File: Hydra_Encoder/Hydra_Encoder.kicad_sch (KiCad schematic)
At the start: 10 parts, among them IC101 AS5600-ASOT, J101 Conn_01x04

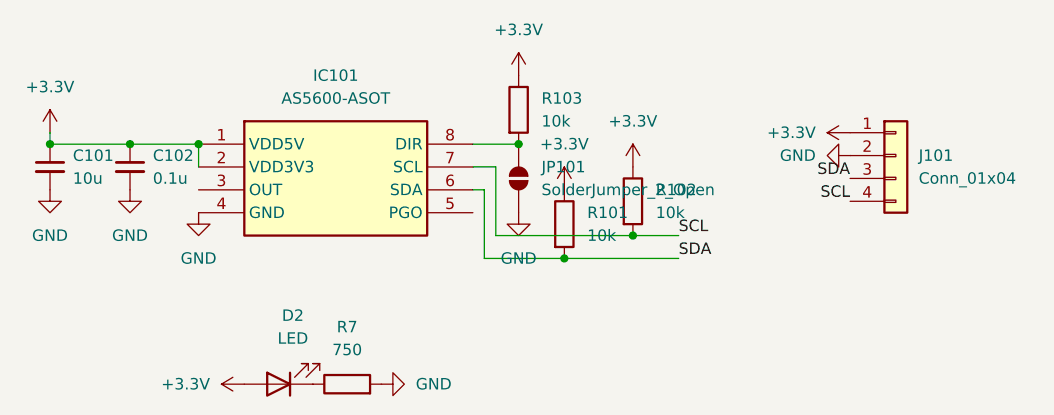
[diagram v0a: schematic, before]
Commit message: Fixed issues preparing for build
Fixed XT30 connectors on Hydra_Driver reversed, fixed I2C connector pin order, refined silkscreens
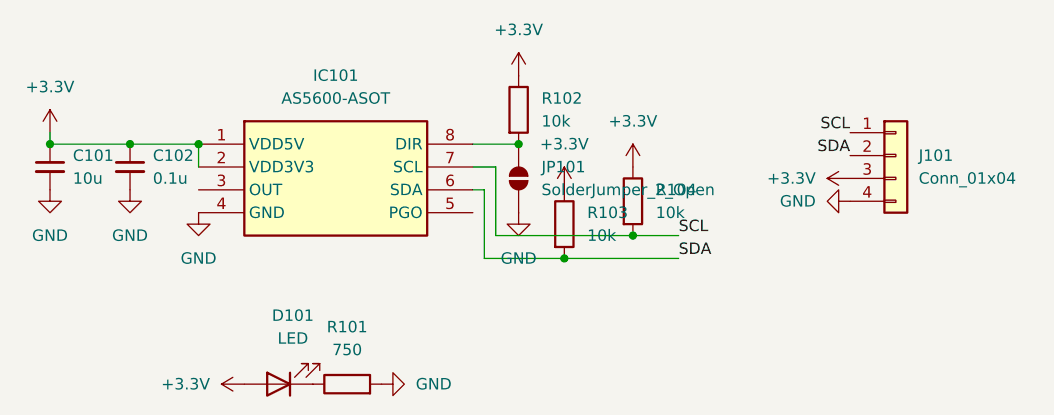
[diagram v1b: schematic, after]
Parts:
- renumbered D2 to D101, R7 to R101, R103 to R102, R101 to R103, R102 to R104
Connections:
- net +3.3V: now also J101.3 (Pin_3); no longer J101.1 (Pin_1)
- net GND: now also J101.4 (Pin_4); no longer J101.2 (Pin_2)
- net SCL: now also J101.1 (Pin_1); no longer J101.4 (Pin_4)
- net SDA: now also J101.2 (Pin_2); no longer J101.3 (Pin_3)
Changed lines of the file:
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@@
 	)
 	(label "SDA"
-		(at 115.57 39.37 180)
+		(at 115.57 36.83 180)
 		(effects
 			(font
@@
 	)
 	(label "SCL"
-		(at 115.57 41.91 180)
+		(at 115.57 34.29 180)
 		(effects
 			(font
@@
 		(dnp no)
 		(fields_autoplaced yes)
-		(property "Reference" "R101"
+		(property "Reference" "R103"
 			(at 86.36 43.1799 0)
 			(effects
@@
 			(project ""
 				(path "/e16511bf-512b-475d-aead-9861d1dac631"
-					(reference "R101")
+					(reference "R103")
 					(unit 1)
 				)
@@
 		(dnp no)
 		(fields_autoplaced yes)
-		(property "Reference" "#PWR0104"
+		(property "Reference" "#PWR0109"
 			(at 83.82 44.45 0)
 			(effects
@@
 			(project ""
 				(path "/e16511bf-512b-475d-aead-9861d1dac631"
-					(reference "#PWR0104")
+					(reference "#PWR0109")
 					(unit 1)
 				)
@@
 		(dnp no)
 		(fields_autoplaced yes)
-		(property "Reference" "#PWR0111"
+		(property "Reference" "#PWR0105"
 			(at 52.07 62.23 0)
 			(effects
@@
 			(project "Hydra_Encoder"
 				(path "/e16511bf-512b-475d-aead-9861d1dac631"
-					(reference "#PWR0111")
+					(reference "#PWR0105")
 					(unit 1)
 				)
@@
 		(dnp no)
 		(fields_autoplaced yes)
-		(property "Reference" "#PWR0108"
+		(property "Reference" "#PWR0103"
 			(at 35.56 46.99 0)
 			(effects
@@
 			(project "Hydra_Encoder"
 				(path "/e16511bf-512b-475d-aead-9861d1dac631"
-					(reference "#PWR0108")
+					(reference "#PWR0103")
 					(unit 1)
 				)
@@
 		(dnp no)
 		(fields_autoplaced yes)
-		(property "Reference" "R7"
+		(property "Reference" "R101"
 			(at 59.69 55.88 90)
 			(effects
@@
 			(project "Hydra_Encoder"
 				(path "/e16511bf-512b-475d-aead-9861d1dac631"
-					(reference "R7")
+					(reference "R101")
 					(unit 1)
 				)
@@
 		(dnp no)
 		(fields_autoplaced yes)
-		(property "Reference" "#PWR0106"
+		(property "Reference" "#PWR0108"
 			(at 78.74 49.53 0)
 			(effects
@@
 			(project "Hydra_Encoder"
 				(path "/e16511bf-512b-475d-aead-9861d1dac631"
-					(reference "#PWR0106")
+					(reference "#PWR0108")
 					(unit 1)
 				)
@@
 		(dnp no)
 		(fields_autoplaced yes)
-		(property "Reference" "R102"
+		(property "Reference" "R104"
 			(at 93.98 40.6399 0)
 			(effects
@@
 			(project ""
 				(path "/e16511bf-512b-475d-aead-9861d1dac631"
-					(reference "R102")
+					(reference "R104")
 					(unit 1)
 				)
@@
 		(dnp no)
 		(fields_autoplaced yes)
-		(property "Reference" "#PWR0103"
+		(property "Reference" "#PWR0107"
 			(at 78.74 31.75 0)
 			(effects
@@
 			(project "Hydra_Encoder"
 				(path "/e16511bf-512b-475d-aead-9861d1dac631"
-					(reference "#PWR0103")
+					(reference "#PWR0107")
 					(unit 1)
 				)
@@
 		(dnp no)
 		(fields_autoplaced yes)
-		(property "Reference" "D2"
+		(property "Reference" "D101"
 			(at 53.6575 54.61 0)
 			(effects
@@
 			(project "Hydra_Encoder"
 				(path "/e16511bf-512b-475d-aead-9861d1dac631"
-					(reference "D2")
+					(reference "D101")
 					(unit 1)
 				)
@@
 		(dnp no)
 		(fields_autoplaced yes)
-		(property "Reference" "#PWR0105"
+		(property "Reference" "#PWR0110"
 			(at 91.44 41.91 0)
 			(effects
@@
 			(project "Hydra_Encoder"
 				(path "/e16511bf-512b-475d-aead-9861d1dac631"
-					(reference "#PWR0105")
+					(reference "#PWR0110")
 					(unit 1)
 				)
@@
 		(dnp no)
 		(fields_autoplaced yes)
-		(property "Reference" "#PWR035"
+		(property "Reference" "#PWR0106"
 			(at 69.85 62.23 0)
 			(effects
@@
 			(project "Hydra_Encoder"
 				(path "/e16511bf-512b-475d-aead-9861d1dac631"
-					(reference "#PWR035")
+					(reference "#PWR0106")
 					(unit 1)
 				)
@@
 		(dnp no)
 		(fields_autoplaced yes)
-		(property "Reference" "R103"
+		(property "Reference" "R102"
 			(at 81.28 30.4799 0)
 			(effects
@@
 			(project "Hydra_Encoder"
 				(path "/e16511bf-512b-475d-aead-9861d1dac631"
-					(reference "R103")
+					(reference "R102")
 					(unit 1)
 				)
@@
 	(symbol
 		(lib_id "power:GND")
-		(at 115.57 36.83 270)
-		(unit 1)
-		(exclude_from_sim no)
-		(in_bom yes)
-		(on_board yes)
-		(dnp no)
-		(fields_autoplaced yes)
-		(property "Reference" "#PWR0110"
-			(at 109.22 36.83 0)
+		(at 115.57 41.91 270)
+		(unit 1)
+		(exclude_from_sim no)
+		(in_bom yes)
+		(on_board yes)
+		(dnp no)
+		(fields_autoplaced yes)
+		(property "Reference" "#PWR0112"
+			(at 109.22 41.91 0)
 			(effects
 				(font
@@
 		)
 		(property "Value" "GND"
-			(at 111.76 36.8299 90)
+			(at 111.76 41.9099 90)
 			(effects
 				(font
@@
 		)
 		(property "Footprint" ""
-			(at 115.57 36.83 0)
+			(at 115.57 41.91 0)
 			(effects
 				(font
@@
 		)
 		(property "Datasheet" ""
-			(at 115.57 36.83 0)
+			(at 115.57 41.91 0)
 			(effects
 				(font
@@
 		)
 		(property "Description" "Power symbol creates a global label with name \"GND\" , ground"
-			(at 115.57 36.83 0)
+			(at 115.57 41.91 0)
 			(effects
 				(font
@@
 			(project "Hydra_Encoder"
 				(path "/e16511bf-512b-475d-aead-9861d1dac631"
-					(reference "#PWR0110")
+					(reference "#PWR0112")
 					(unit 1)
 				)
@@
 		(dnp no)
 		(fields_autoplaced yes)
-		(property "Reference" "#PWR0107"
+		(property "Reference" "#PWR0102"
 			(at 26.67 46.99 0)
 			(effects
@@
 			(project "Hydra_Encoder"
 				(path "/e16511bf-512b-475d-aead-9861d1dac631"
-					(reference "#PWR0107")
+					(reference "#PWR0102")
 					(unit 1)
 				)
@@
 		(dnp no)
 		(fields_autoplaced yes)
-		(property "Reference" "#PWR0102"
+		(property "Reference" "#PWR0104"
 			(at 43.18 49.53 0)
 			(effects
@@
 			(project ""
 				(path "/e16511bf-512b-475d-aead-9861d1dac631"
-					(reference "#PWR0102")
+					(reference "#PWR0104")
 					(unit 1)
 				)
@@
 	(symbol
 		(lib_id "power:+3.3V")
-		(at 115.57 34.29 90)
-		(unit 1)
-		(exclude_from_sim no)
-		(in_bom yes)
-		(on_board yes)
-		(dnp no)
-		(fields_autoplaced yes)
-		(property "Reference" "#PWR0109"
-			(at 119.38 34.29 0)
+		(at 115.57 39.37 90)
+		(unit 1)
+		(exclude_from_sim no)
+		(in_bom yes)
+		(on_board yes)
+		(dnp no)
+		(fields_autoplaced yes)
+		(property "Reference" "#PWR0111"
+			(at 119.38 39.37 0)
 			(effects
 				(font
@@
 		)
 		(property "Value" "+3.3V"
-			(at 111.76 34.2899 90)
+			(at 111.76 39.3699 90)
 			(effects
 				(font
@@
 		)
 		(property "Footprint" ""
-			(at 115.57 34.29 0)
+			(at 115.57 39.37 0)
 			(effects
 				(font
@@
 		)
 		(property "Datasheet" ""
-			(at 115.57 34.29 0)
+			(at 115.57 39.37 0)
 			(effects
 				(font
@@
 		)
 		(property "Description" "Power symbol creates a global label with name \"+3.3V\""
-			(at 115.57 34.29 0)
+			(at 115.57 39.37 0)
 			(effects
 				(font
@@
 			(project "Hydra_Encoder"
 				(path "/e16511bf-512b-475d-aead-9861d1dac631"
-					(reference "#PWR0109")
-					(unit 1)
-				)
+					(reference "#PWR0111")
+					(unit 1)
+				)

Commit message: More changes to start production
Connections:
- net +3.3V: now also JP101.2 (B); no longer R102.1
- net GND: now also R102.2; no longer JP101.1 (A)
- new net: IC101.8 (DIR), JP101.1 (A), R102.1
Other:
- moved on the sheet: JP101, R102
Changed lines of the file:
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@@
+	)
+	(junction
+		(at 78.74 35.56)
+		(diameter 0)
+		(color 0 0 0 0)
 	)
 	(junction
@@
 	(junction
 		(at 26.67 35.56)
-		(diameter 0)
-		(color 0 0 0 0)
-	)
-	(junction
-		(at 78.74 35.56)
 		(diameter 0)
 		(color 0 0 0 0)
@@
 	(symbol
 		(lib_id "Jumper:SolderJumper_2_Open")
-		(at 78.74 39.37 90)
+		(at 78.74 31.75 90)
 		(unit 1)
 		(exclude_from_sim no)
@@
 		(fields_autoplaced yes)
 		(property "Reference" "JP101"
-			(at 81.28 38.0999 90)
+			(at 81.28 30.4799 90)
 			(effects
 				(font
@@
 		)
 		(property "Value" "SolderJumper_2_Open"
-			(at 81.28 40.6399 90)
+			(at 81.28 33.0199 90)
 			(effects
 				(font
@@
 		)
 		(property "Footprint" "Jumper:SolderJumper-2_P1.3mm_Open_RoundedPad1.0x1.5mm"
-			(at 78.74 39.37 0)
+			(at 78.74 31.75 0)
 			(effects
 				(font
@@
 		)
 		(property "Datasheet" "~"
-			(at 78.74 39.37 0)
+			(at 78.74 31.75 0)
 			(effects
 				(font
@@
 		)
 		(property "Description" "Solder Jumper, 2-pole, open"
-			(at 78.74 39.37 0)
+			(at 78.74 31.75 0)
 			(effects
 				(font
@@
 	(symbol
 		(lib_id "Device:R")
-		(at 78.74 31.75 0)
+		(at 78.74 39.37 0)
 		(unit 1)
 		(exclude_from_sim no)
@@
 		(fields_autoplaced yes)
 		(property "Reference" "R102"
-			(at 81.28 30.4799 0)
+			(at 81.28 38.0999 0)
 			(effects
 				(font
@@
 		)
 		(property "Value" "10k"
-			(at 81.28 33.0199 0)
+			(at 81.28 40.6399 0)
 			(effects
 				(font
@@
 		)
 		(property "Footprint" "Resistor_SMD:R_0402_1005Metric"
-			(at 76.962 31.75 90)
+			(at 76.962 39.37 90)
 			(effects
 				(font
@@
 		)
 		(property "Datasheet" "~"
-			(at 78.74 31.75 0)
+			(at 78.74 39.37 0)
 			(effects
 				(font
@@
 		)
 		(property "Description" "Resistor"
-			(at 78.74 31.75 0)
-			(effects
-				(font
+			(at 78.74 39.37 0)
+			(effects
+				(font
